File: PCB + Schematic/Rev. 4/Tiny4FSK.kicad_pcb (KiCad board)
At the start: 4 copper layers, 22.8 x 69.4 mm, 71 parts, among them IC1 SI4063, J1 SWD, J2 GPIO, J4 USB, J5 I2C, J6 Power, J7 SPI, SW1 RST, SW2 BATT PWR, U1 BME280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

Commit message: Smaller footprints, resize board
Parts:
- AE1: value GPS ANT -> GPS1003
- C10, C12, C15, C16, C18, C2, C21, C8, C9: footprint Capacitor_SMD:C_0805_2012Metric_Pad1.18x1.45mm_HandSolder -> Capacitor_SMD:C_0402_1005Metric_Pad0.74x0.62mm_HandSolder
- C13, C14, C28, C7: footprint Capacitor_SMD:C_0805_2012Metric_Pad1.18x1.45mm_HandSolder -> Capacitor_SMD:C_0603_1608Metric_Pad1.08x0.95mm_HandSolder
- C20: footprint Capacitor_SMD:C_0603_1608Metric_Pad1.08x0.95mm_HandSolder -> Capacitor_SMD:C_0402_1005Metric_Pad0.74x0.62mm_HandSolder
- C24: value 10 nF -> 100 nF; footprint Capacitor_SMD:C_0805_2012Metric_Pad1.18x1.45mm_HandSolder -> Capacitor_SMD:C_0402_1005Metric_Pad0.74x0.62mm_HandSolder
- R10, R13, R9: value 100 -> 330; footprint Resistor_SMD:R_0805_2012Metric_Pad1.20x1.40mm_HandSolder -> Resistor_SMD:R_0603_1608Metric_Pad0.98x0.95mm_HandSolder
- R4: footprint Resistor_SMD:R_0805_2012Metric_Pad1.20x1.40mm_HandSolder -> Resistor_SMD:R_0402_1005Metric_Pad0.72x0.64mm_HandSolder
- R6, R8: footprint Resistor_SMD:R_0805_2012Metric_Pad1.20x1.40mm_HandSolder -> Resistor_SMD:R_0603_1608Metric_Pad0.98x0.95mm_HandSolder
- U5: value TCXO MCU -> 1XZA032768AD19
- moved H1 8.90 mm to (135.2, 40.8)
- moved AE1 5.75 mm to (157.2, 46.1)
- moved C9 3.01 mm to (151.2, 76.8), turned to -90 degrees
- moved U1 1.58 mm to (142.4, 52.1)
- moved U2 1.50 mm to (152.8, 56.5)
- moved C8 1.40 mm to (149.7, 76.1)
- moved L1 1.25 mm to (155.2, 49.8)
- moved C21 1.12 mm to (155.9, 66.5)
- moved C13 1.06 mm to (149.1, 69.8)
- moved R1 1.01 mm to (142.5, 54.5)
- moved C16 1.00 mm to (156.9, 69.8)
- moved L2 1.00 mm to (150.8, 65.0)
- moved R11 1.00 mm to (155.5, 73.0)
- moved R12 1.00 mm to (151.5, 73.0)
- moved R2 1.00 mm to (145.0, 51.5)
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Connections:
- U2 pad 5: Earth -> GPS_EN
- U4 pad 11: unconnected-(U4-PA06-Pad11) -> GPS_EN
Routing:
- net +3.3V: track 74.4 -> 79.3 mm, vias 18 -> 19
- net Earth: track 44.5 -> 40.4 mm, vias 44 -> 41
- net ANT_GPS: track 8.33 -> 5.60 mm
- net TXD: track 43.1 -> 45.8 mm
- net RXD: track 45.9 -> 48.5 mm
- net ERROR: track 30.9 -> 29.0 mm
- net BST_IN: track 13.5 -> 14.8 mm
- net Net-(U1-CSB): track 3.69 -> 2.74 mm
- net nRST: track 36.8 -> 36.0 mm
- net Net-(U6-VAUX): track 1.82 -> 2.64 mm
- net +BATT: track 28.7 -> 28.3 mm, vias 2 -> 3
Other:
- board size 22.8 x 69.4 mm -> 22.8 x 63.7 mm

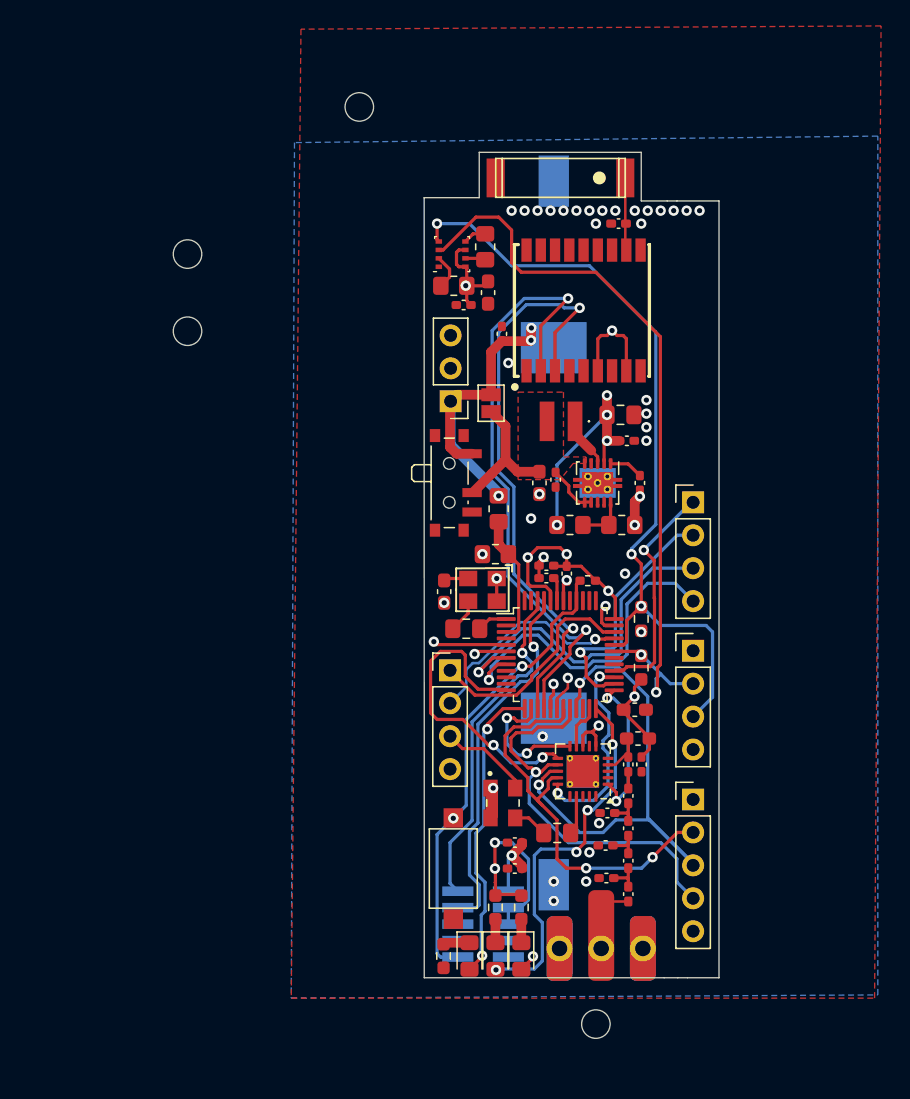
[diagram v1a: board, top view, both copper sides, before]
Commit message: Update PCB, add more jlcpcb parts
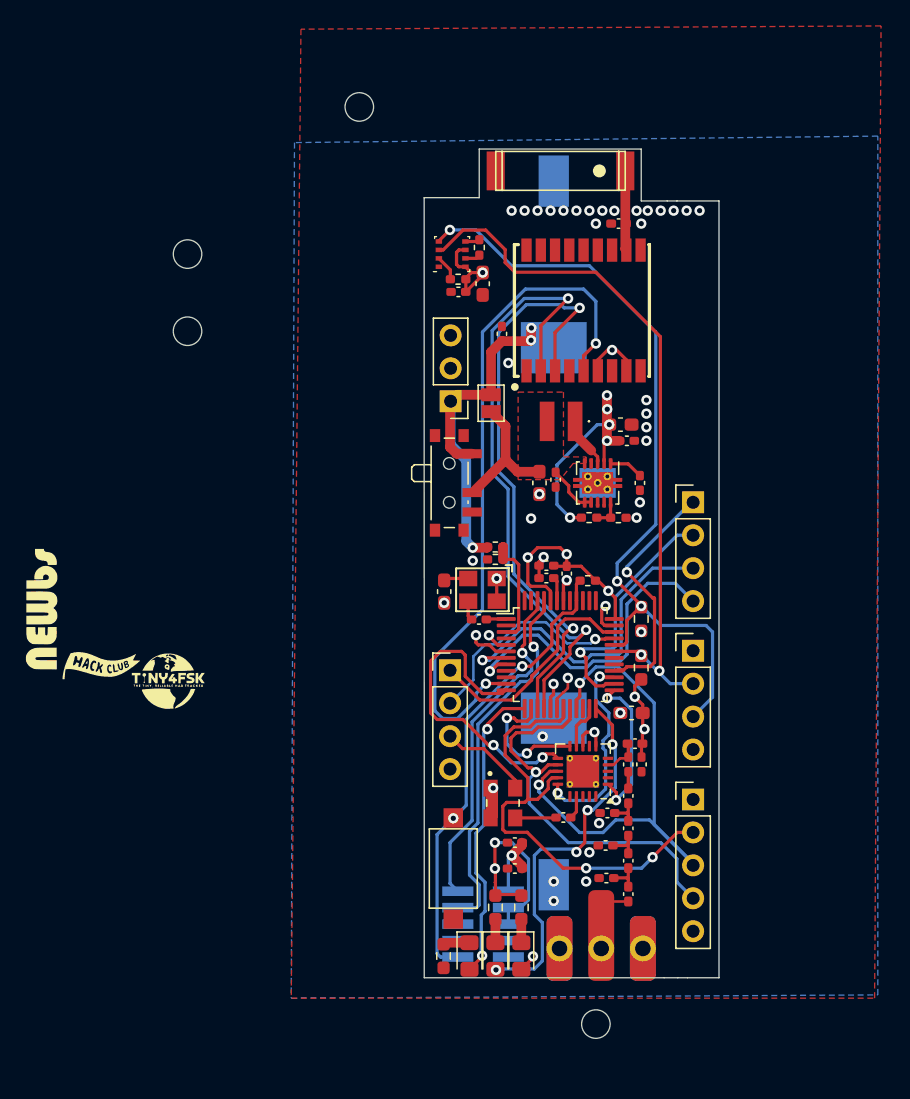
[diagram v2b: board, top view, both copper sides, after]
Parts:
- added G***: LOGO, LOGO, F.Cu at (120.5, 85.0)
- C11, C23: footprint Capacitor_SMD:C_0805_2012Metric_Pad1.18x1.45mm_HandSolder -> Capacitor_SMD:C_0402_1005Metric_Pad0.74x0.62mm_HandSolder
- C17: footprint Capacitor_SMD:C_0805_2012Metric_Pad1.18x1.45mm_HandSolder -> Capacitor_SMD:C_0603_1608Metric_Pad1.08x0.95mm_HandSolder
- G*** (x2): moved to F.Cu
- L3: footprint Inductor_SMD:L_0603_1608Metric_Pad1.05x0.95mm_HandSolder -> Inductor_SMD:L_0402_1005Metric_Pad0.77x0.64mm_HandSolder
- R1, R11, R12, R14, R15, R2: footprint Resistor_SMD:R_0805_2012Metric_Pad1.20x1.40mm_HandSolder -> Resistor_SMD:R_0402_1005Metric_Pad0.72x0.64mm_HandSolder
- moved G*** 22.1 mm to (115.4, 83.8), turned to 0 degrees
- moved G*** 21.9 mm to (98.4, 68.8)
- moved G*** 6.75 mm to (110.8, 79.5), turned to 90 degrees
- moved R14 2.96 mm to (145.7, 74.7), turned to 0 degrees
- moved R12 1.58 mm to (153.0, 72.4)
- moved C23 1.29 mm to (151.0, 95.6)
- moved C11 1.21 mm to (144.5, 80.3)
- moved C2 1.09 mm to (142.9, 55.0)
- moved C28 0.80 mm to (144.8, 54.4)
- moved C17 0.75 mm to (155.4, 65.3)
- moved R11 0.62 mm to (155.2, 72.4)
- moved R1 0.61 mm to (142.9, 54.0)
- moved AE1 0.54 mm to (157.2, 45.6)
- moved L3 0.46 mm to (156.5, 89.9)
- moved R2 0.46 mm to (144.5, 51.6)
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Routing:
- net GPS_EN: track 0.00 -> 54.2 mm, vias 0 -> 2
- net Earth: track 40.4 -> 33.6 mm, vias 41 -> 42
- net SDA: track 59.7 -> 54.8 mm
- net +BATT: track 28.3 -> 32.6 mm
- net MOSI: track 32.1 -> 35.8 mm
- net +3.3V: track 79.3 -> 76.3 mm, vias 19 -> 20
- net Net-(U6-FB): track 3.83 -> 1.99 mm
- net BATT_SENSE: track 9.97 -> 8.36 mm
- net A1: track 27.0 -> 25.6 mm
- net A2: track 26.4 -> 25.0 mm
- net Net-(IC1-XIN): track 3.01 -> 1.81 mm
- net D12: track 17.6 -> 18.8 mm
- net Net-(U5-OUTPUT): track 2.54 -> 1.45 mm
- net TCXO: track 2.36 -> 1.55 mm
- net Net-(U1-CSB): track 2.74 -> 1.98 mm
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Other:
- board size 22.8 x 63.7 mm -> 22.8 x 63.9 mm

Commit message: Neaten up schematic, add breakaway tabs and stitching vias
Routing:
- net SDA: track 54.8 -> 59.6 mm
- net MISO: track 41.2 -> 37.3 mm
- net MOSI: track 35.8 -> 36.8 mm
- net A2: track 25.0 -> 26.0 mm
- net D12: track 18.8 -> 19.6 mm
- net SCK: track 30.8 -> 30.3 mm
- net Earth: track 33.6 -> 33.9 mm, vias 42 -> 131
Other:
- outline, holes or cut-outs redrawn

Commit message: Gerbers, stitching, SLP
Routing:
- net Earth: track 33.9 -> 40.1 mm, vias 131 -> 143
- net +BATT: track 32.6 -> 30.3 mm, vias 3 -> 5
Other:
- outline, holes or cut-outs redrawn

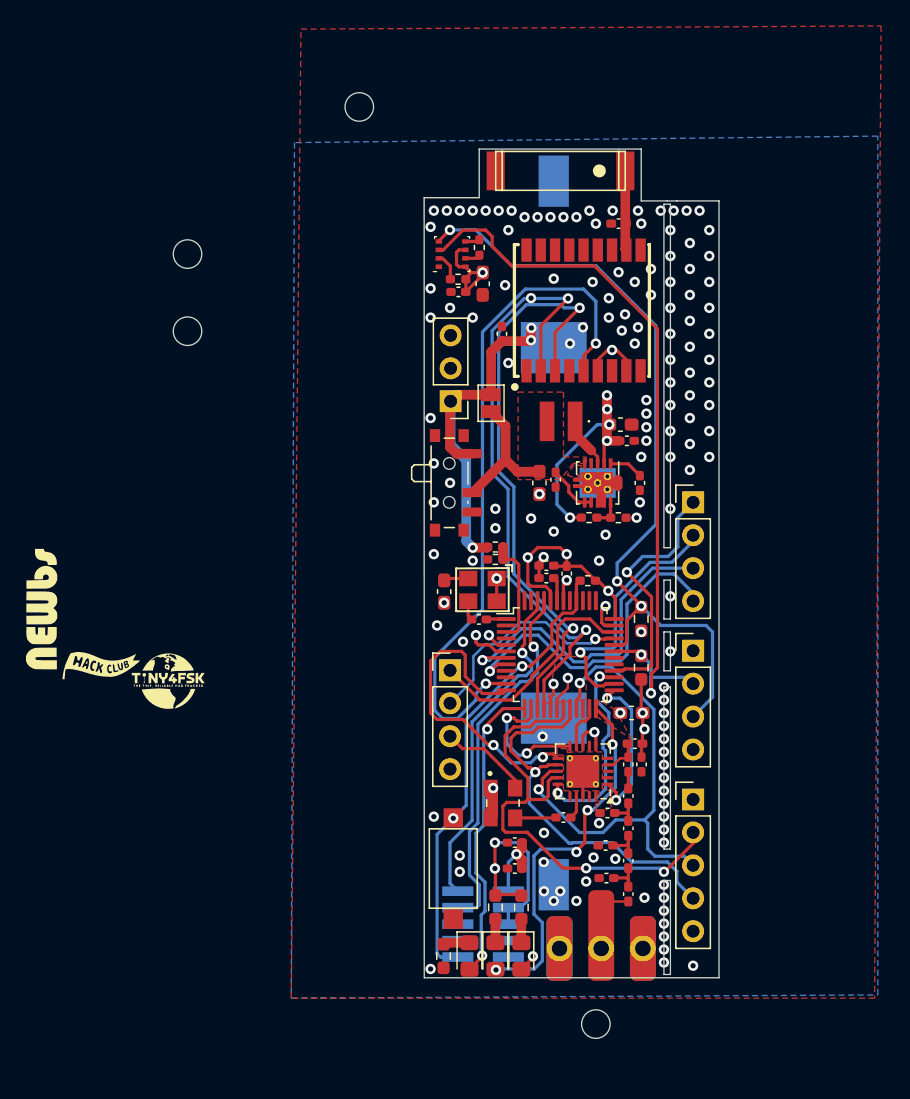
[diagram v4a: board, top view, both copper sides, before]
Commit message: Fix breakaway, mounting holes
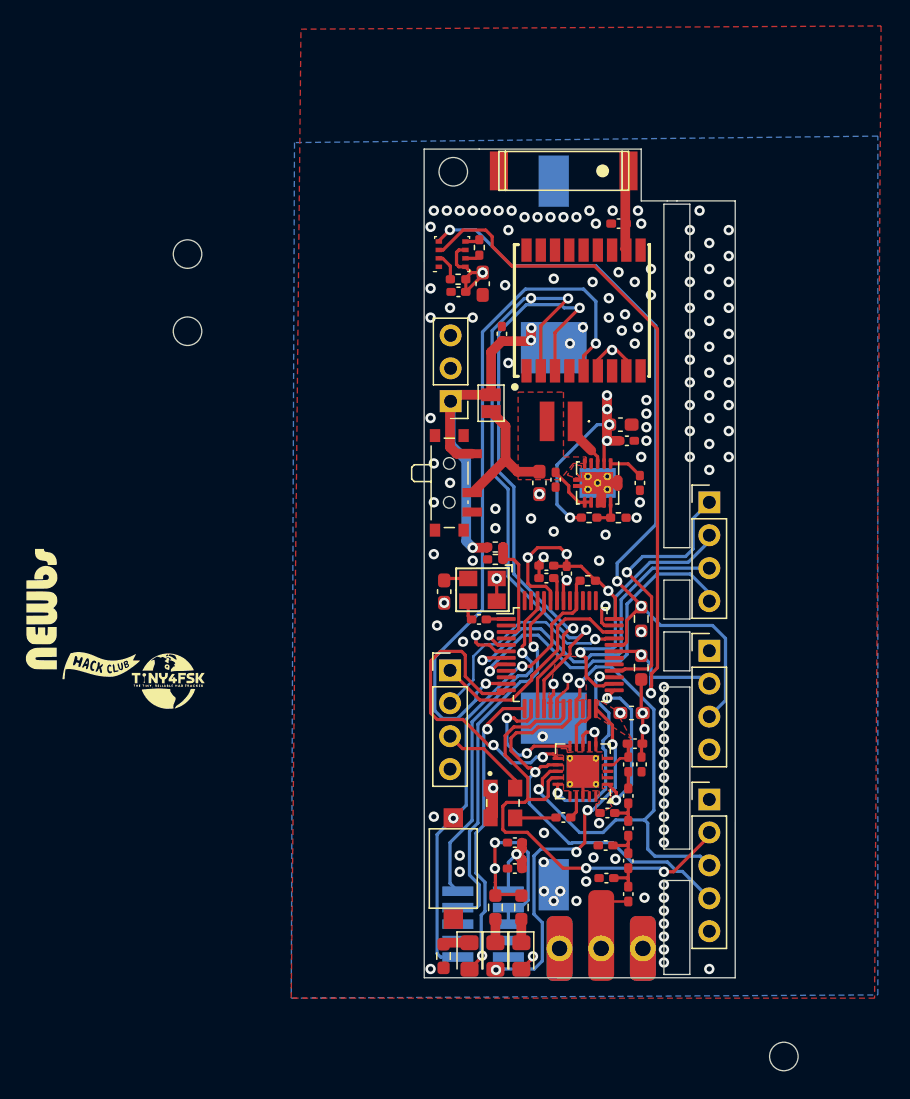
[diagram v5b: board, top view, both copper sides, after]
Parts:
- moved H4 14.7 mm to (168.0, 114.0)
- moved H1 8.81 mm to (142.5, 45.8)
- moved J2 1.25 mm to (162.2, 71.2)
- moved J5 1.25 mm to (162.2, 82.7)
- moved J7 1.25 mm to (162.2, 94.2)
- moved AE1 0.25 mm to (157.5, 45.6)
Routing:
- net D12: track 19.6 -> 20.9 mm
- net SDA: track 59.6 -> 60.8 mm
- net MISO: track 37.3 -> 38.5 mm
- net D13: track 19.5 -> 20.7 mm
- net A2: track 26.0 -> 27.2 mm
- net A1: track 25.6 -> 26.8 mm
- net MOSI: track 36.8 -> 37.7 mm
- net SCK: track 30.3 -> 31.1 mm
- net SCL: track 61.6 -> 62.2 mm
- net Earth: vias 143 -> 137
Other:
- board size 22.8 x 63.9 mm -> 24 x 63.9 mm

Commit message: Neaten up reference designators
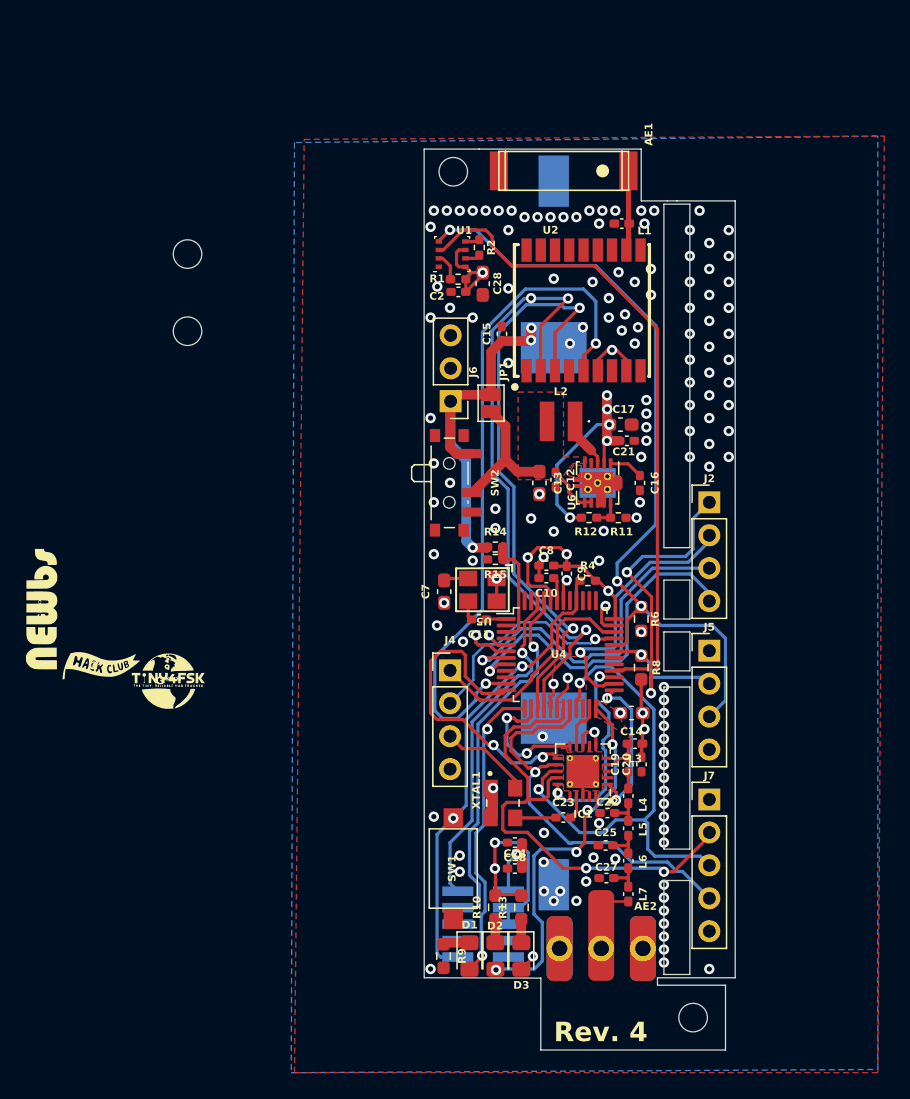
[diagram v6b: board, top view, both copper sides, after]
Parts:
- moved H4 7.62 mm to (161.0, 111.0)
- moved L1 0.25 mm to (155.5, 49.8)
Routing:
- net Earth: vias 137 -> 138
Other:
- board size 24 x 63.9 mm -> 24 x 69.5 mm
- board text added: "Rev. 4"

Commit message: Reference designators
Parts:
- AE2: value ANT -> TX Antenna
- BT1: value Battery_Cell -> BK-53
- J6: value Power -> Power Ext
- JP1: value SWITCH_EN -> Switch EN
- SW2: value BATT PWR -> Power Switch
- moved H4 18.5 mm to (142.5, 111.0)
- moved C16 0.75 mm to (156.1, 69.8)
- renumbered IC1 to U3, XTAL1 to U7
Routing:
- net +3.3V: track 75.8 -> 72.2 mm
- net SCL: track 62.2 -> 63.3 mm
- net Net-(U6-VAUX): track 2.64 -> 1.89 mm
- net Earth: track 40.1 -> 40.4 mm, vias 138 -> 136
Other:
- outline, holes or cut-outs redrawn
- board text removed: "Rev. 4"
